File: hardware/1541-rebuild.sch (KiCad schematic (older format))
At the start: 12 parts, among them IC1 ATMEGA1284P-P, J1 ISP, J2 KEYS, J3 EXT_5V, J4 RESET CONN, J5 PC7, SW1 RESET, X1 24Mhz

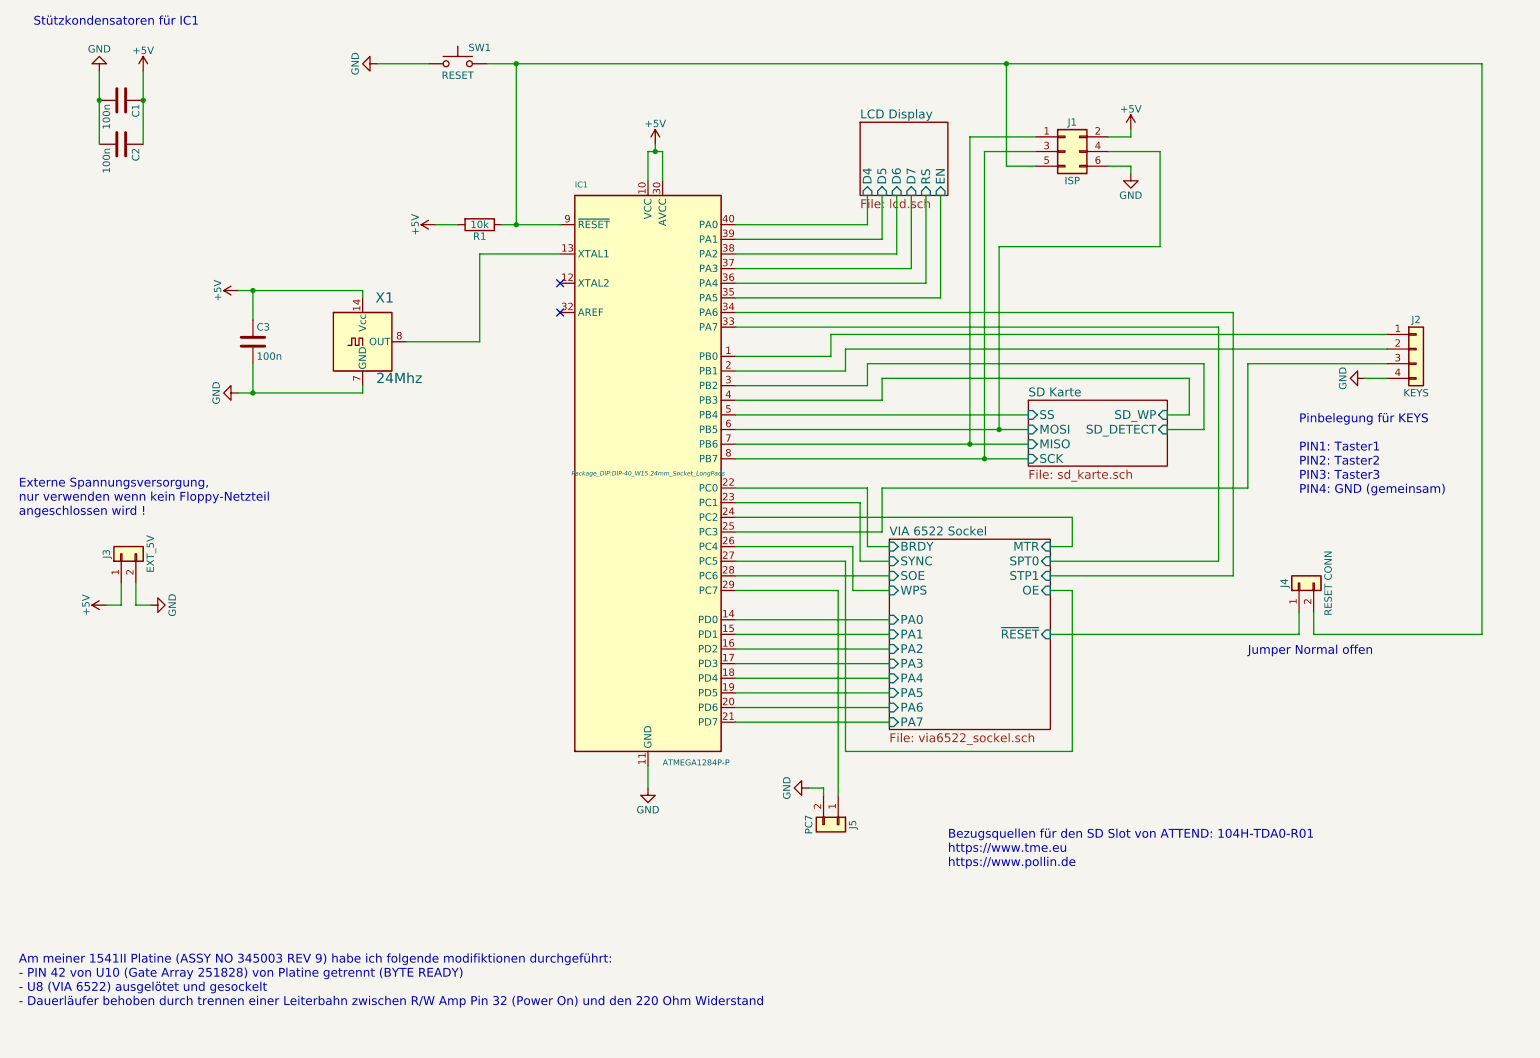
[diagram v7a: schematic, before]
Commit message: Schaltplan angepasst: - SD Card Slot entfernt - SD Card Modul Connector hinzugefügt - im PCB alle Leiterbahne entfernt
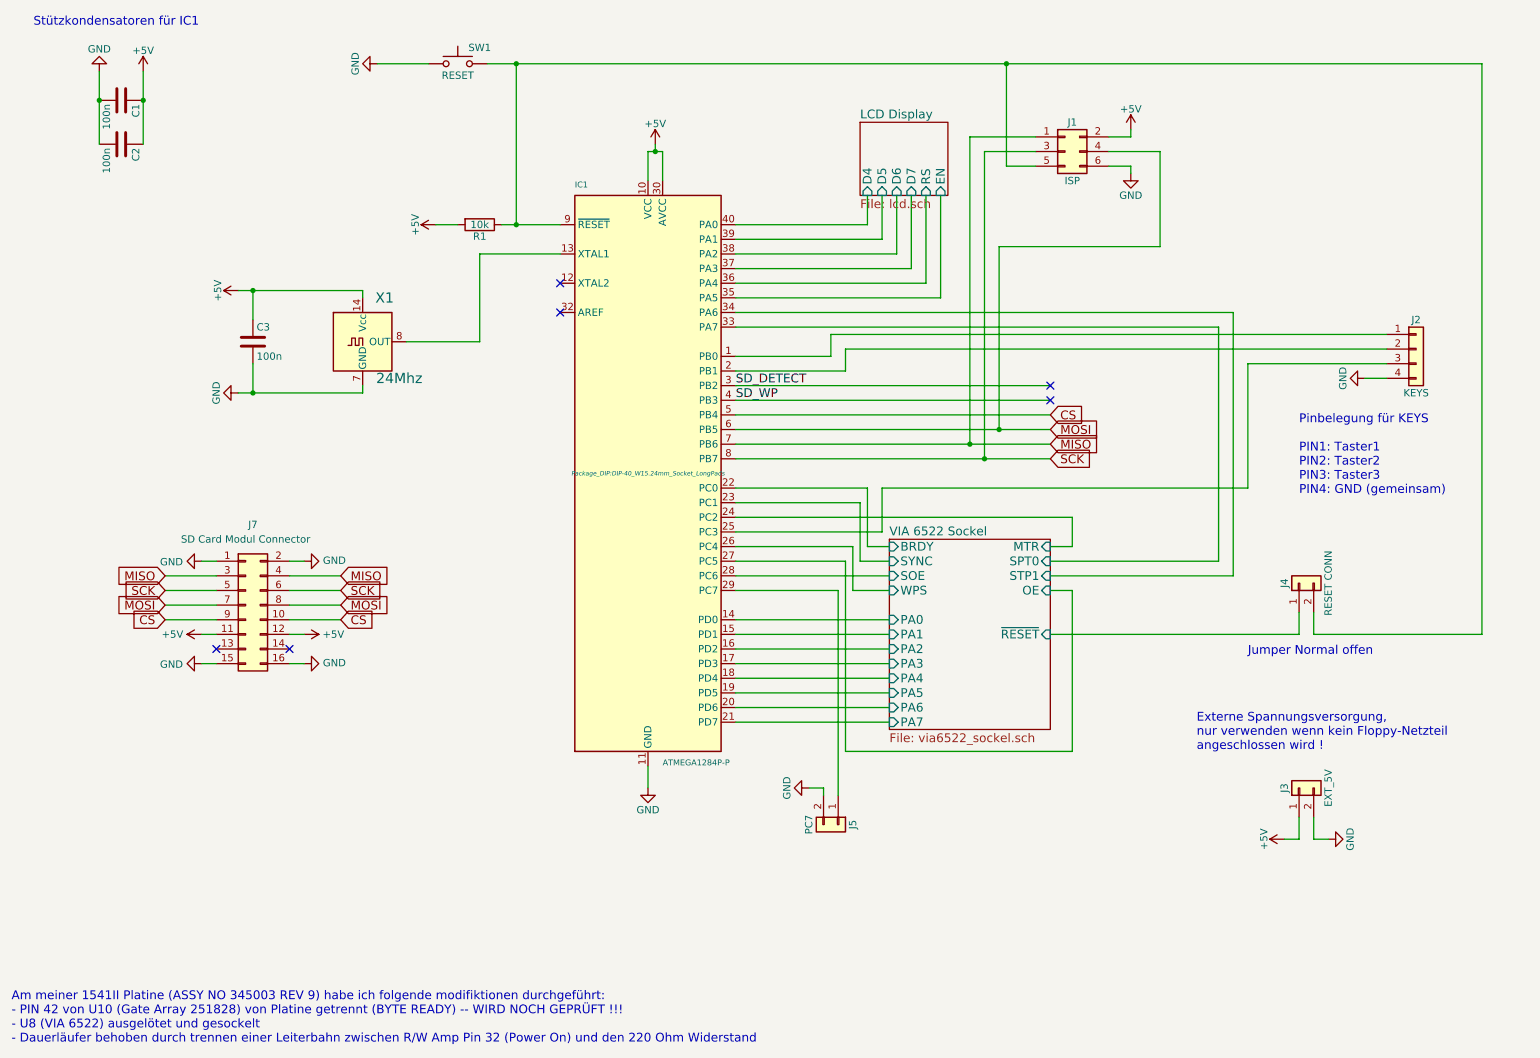
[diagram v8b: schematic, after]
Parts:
- added J7: SD Card Modul Connector, Connector_PinSocket_2.54mm:PinSocket_2x08_P2.54mm_Vertical, symbol Connector_Generic:Conn_02x08_Odd_Even
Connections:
- net +5V: now also J7.11 (Pin_11), J7.12 (Pin_12)
- net GND: now also J7.1 (Pin_1), J7.15 (Pin_15), J7.16 (Pin_16), J7.2 (Pin_2)
- net SD Karte/MISO renamed MISO
- net MISO: now also J7.3 (Pin_3), J7.4 (Pin_4)
- net SD Karte/MOSI renamed MOSI
- net MOSI: now also J7.7 (Pin_7), J7.8 (Pin_8)
- net SD Karte/SCK renamed SCK
- net SCK: now also J7.5 (Pin_5), J7.6 (Pin_6)
- net SD Karte/SD_DETECT renamed SD_DETECT
- net SD Karte/SD_WP renamed SD_WP
- net SD Karte/SS renamed CS
- net CS: now also J7.10 (Pin_10), J7.9 (Pin_9)
- no-connect marks 2 -> 6
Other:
- note added: "Am meiner 1541II Platine (ASSY NO 345003 REV 9) habe ich folgende modifiktionen durchgeführt:\n- PIN 42 von U10 (Gate Array 251828) von Platine getrennt (BYTE READY) -- WIRD NOCH GEPRÜFT !!!\n- U8 (VIA 6522) ausgelötet und gesockelt\n- Dauerläufer behoben durch trennen einer Leiterbahn zwischen R/W Amp Pin 32 (Power On) und den 220 Ohm Widerstand"
- note removed: "Am meiner 1541II Platine (ASSY NO 345003 REV 9) habe ich folgende modifiktionen durchgeführt:\n- PIN 42 von U10 (Gate Array 251828) von Platine getrennt (BYTE READY)\n- U8 (VIA 6522) ausgelötet und gesockelt\n- Dauerläufer behoben durch trennen einer Leiterbahn zwischen R/W Amp Pin 32 (Power On) und den 220 Ohm Widerstand"
- note removed: "Bezugsquellen für den SD Slot von ATTEND: 104H-TDA0-R01\nhttps://www.tme.eu\nhttps://www.pollin.de\n"
- moved on the sheet: J3
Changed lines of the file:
@@
 $Descr A4 11693 8268
 encoding utf-8
-Sheet 1 4
+Sheet 1 3
 Title "1541-rebuid"
 Date "2020-04-14"
@@
 	1    0    0    -1
 $EndComp
-Text Notes 650  7450 0    60   ~ 0
-Am meiner 1541II Platine (ASSY NO 345003 REV 9) habe ich folgende modifiktionen durchgeführt:\n- PIN 42 von U10 (Gate Array 251828) von Platine getrennt (BYTE READY)\n- U8 (VIA 6522) ausgelötet und gesockelt\n- Dauerläufer behoben durch trennen einer Leiterbahn zwischen R/W Amp Pin 32 (Power On) und den 220 Ohm Widerstand
+Text Notes 600  7700 0    60   ~ 0
+Am meiner 1541II Platine (ASSY NO 345003 REV 9) habe ich folgende modifiktionen durchgeführt:\n- PIN 42 von U10 (Gate Array 251828) von Platine getrennt (BYTE READY) -- WIRD NOCH GEPRÜFT !!!\n- U8 (VIA 6522) ausgelötet und gesockelt\n- Dauerläufer behoben durch trennen einer Leiterbahn zwischen R/W Amp Pin 32 (Power On) und den 220 Ohm Widerstand
 $Comp
 L Oscillator:TCXO-14 X1
@@
 Text Notes 750  750  0    60   ~ 0
 Stützkondensatoren für IC1
-$Sheet
-S 7550 3300 950  450
-U 55F7A0F9
-F0 "SD Karte" 60
-F1 "sd_karte.sch" 60
-F2 "MISO" I L 7550 3600 60
-F3 "SCK" I L 7550 3700 60
-F4 "MOSI" I L 7550 3500 60
-F5 "SS" I L 7550 3400 60
-F6 "SD_DETECT" I R 8500 3500 60
-F7 "SD_WP" I R 8500 3400 60
-$EndSheet
 $Sheet
 S 6400 1400 600  500
@@
 	7850 4300 7700 4300
 Wire Wire Line
-	5550 3400 7550 3400
+	5550 3400 7700 3400
 Wire Wire Line
 	5550 3500 7350 3500
@@
 	5550 3700 7250 3700
 Wire Wire Line
-	5550 3300 6550 3300
-Wire Wire Line
-	6550 3300 6550 3150
-Wire Wire Line
-	6550 3150 8650 3150
-Wire Wire Line
-	8650 3150 8650 3400
-Wire Wire Line
-	8650 3400 8500 3400
-Wire Wire Line
-	5550 3200 6450 3200
-Wire Wire Line
-	6450 3200 6450 3050
-Wire Wire Line
-	6450 3050 8750 3050
-Wire Wire Line
-	8750 3050 8750 3500
-Wire Wire Line
-	8750 3500 8500 3500
+	5550 3300 7700 3300
+Wire Wire Line
+	5550 3200 7700 3200
 Wire Wire Line
 	5550 3000 6200 3000
@@
 Wire Wire Line
 	6300 3100 6300 2950
-Wire Wire Line
-	6300 2950 10000 2950
 Wire Wire Line
 	5550 4200 6550 4200
@@
 L Connector_Generic:Conn_01x02 J3
 U 1 1 5AEF69AF
-P 1350 4350
-F 0 "J3" H 1350 4450 50  0000 C CNN
-F 1 "EXT_5V" H 1350 4150 50  0000 C CNN
-F 2 "Connector_PinHeader_2.54mm:PinHeader_1x02_P2.54mm_Vertical" H 1350 4350 50  0001 C CNN
-F 3 "" H 1350 4350 50  0001 C CNN
-	1    1350 4350
+P 9400 5950
+F 0 "J3" H 9400 6050 50  0000 C CNN
+F 1 "EXT_5V" H 9400 5750 50  0000 C CNN
+F 2 "Connector_PinHeader_2.54mm:PinHeader_1x02_P2.54mm_Vertical" H 9400 5950 50  0001 C CNN
+F 3 "" H 9400 5950 50  0001 C CNN
+	1    9400 5950
 	0    -1   -1   0
 $EndComp
@@
 L power:+5V #PWR06
 U 1 1 5AEF757D
-P 1250 4700
-F 0 "#PWR06" H 1250 4550 50  0001 C CNN
-F 1 "+5V" H 1250 4840 50  0000 C CNN
-F 2 "" H 1250 4700 60  0000 C CNN
-F 3 "" H 1250 4700 60  0000 C CNN
-	1    1250 4700
-	0    -1   -1   0
-$EndComp
-Wire Wire Line
-	1350 4550 1350 4700
-Wire Wire Line
-	1450 4700 1450 4550
-Wire Wire Line
-	1350 4700 1250 4700
-Wire Wire Line
-	1450 4700 1550 4700
-Text Notes 650  4100 0    60   ~ 0
+P 9300 6300
+F 0 "#PWR06" H 9300 6150 50  0001 C CNN
+F 1 "+5V" H 9300 6440 50  0000 C CNN
+F 2 "" H 9300 6300 60  0000 C CNN
+F 3 "" H 9300 6300 60  0000 C CNN
+	1    9300 6300
+	0    -1   -1   0
+$EndComp
+Wire Wire Line
+	9400 6150 9400 6300
+Wire Wire Line
+	9500 6300 9500 6150
+Wire Wire Line
+	9400 6300 9300 6300
+Wire Wire Line
+	9500 6300 9600 6300
+Text Notes 8700 5700 0    60   ~ 0
 Externe Spannungsversorgung,\nnur verwenden wenn kein Floppy-Netzteil\nangeschlossen wird !
 Wire Wire Line
@@
 L power:GND #PWR010
 U 1 1 5AF0A9E7
-P 1550 4700
-F 0 "#PWR010" H 1550 4450 50  0001 C CNN
-F 1 "GND" H 1550 4550 50  0000 C CNN
-F 2 "" H 1550 4700 50  0001 C CNN
-F 3 "" H 1550 4700 50  0001 C CNN
-	1    1550 4700
+P 9600 6300
+F 0 "#PWR010" H 9600 6050 50  0001 C CNN
+F 1 "GND" H 9600 6150 50  0000 C CNN
+F 2 "" H 9600 6300 50  0001 C CNN
+F 3 "" H 9600 6300 50  0001 C CNN
+	1    9600 6300
 	0    -1   -1   0
 $EndComp
@@
 Wire Wire Line
 	6150 5950 6150 6000
-Text Notes 7000 6500 0    60   ~ 0
-Bezugsquellen für den SD Slot von ATTEND: 104H-TDA0-R01\nhttps://www.tme.eu\nhttps://www.pollin.de\n
 Wire Wire Line
 	5000 1600 5050 1600
@@
 	1500 1250 1500 1550
 Wire Wire Line
-	7150 3600 7550 3600
-Wire Wire Line
-	7250 3700 7550 3700
+	7150 3600 7700 3600
+Wire Wire Line
+	7250 3700 7700 3700
 Wire Wire Line
 	4050 2100 4350 2100
 Wire Wire Line
-	7350 3500 7550 3500
+	7350 3500 7700 3500
 Wire Wire Line
 	7400 1000 10650 1000
@@
 Wire Wire Line
 	2250 3250 3000 3250
+Wire Wire Line
+	6300 2950 10000 2950
+$Comp
+L Connector_Generic:Conn_02x08_Odd_Even J7
+U 1 1 5E991479
+P 2200 4700
+F 0 "J7" H 2250 5250 50  0000 C CNN
+F 1 "SD Card Modul Connector" H 2200 5150 50  0000 C CNN
+F 2 "Connector_PinSocket_2.54mm:PinSocket_2x08_P2.54mm_Vertical" H 2200 4700 50  0001 C CNN
+F 3 "~" H 2200 4700 50  0001 C CNN
+	1    2200 4700
+	1    0    0    -1
+$EndComp
+Text GLabel 1650 4500 0    60   Input ~ 0
+MISO
+Text GLabel 2850 4500 2    60   Input ~ 0
+MISO
+Wire Wire Line
+	1650 4500 2000 4500
+Wire Wire Line
+	2500 4500 2850 4500
+$Comp
+L power:GND #PWR0106
+U 1 1 5E9BBC13
+P 2600 5100
+F 0 "#PWR0106" H 2600 4850 50  0001 C CNN
+F 1 "GND" V 2605 4972 50  0000 R CNN
+F 2 "" H 2600 5100 50  0001 C CNN
+F 3 "" H 2600 5100 50  0001 C CNN
+	1    2600 5100
+	0    -1   -1   0
+$EndComp
+$Comp
+L power:GND #PWR0107
+U 1 1 5E9BC3F8
+P 1900 5100
+F 0 "#PWR0107" H 1900 4850 50  0001 C CNN
+F 1 "GND" V 1905 4972 50  0000 R CNN
+F 2 "" H 1900 5100 50  0001 C CNN
+F 3 "" H 1900 5100 50  0001 C CNN
+	1    1900 5100
+	0    1    1    0
+$EndComp
+$Comp
+L power:GND #PWR0108
+U 1 1 5E9BC951
+P 1900 4400
+F 0 "#PWR0108" H 1900 4150 50  0001 C CNN
+F 1 "GND" V 1905 4272 50  0000 R CNN
+F 2 "" H 1900 4400 50  0001 C CNN
+F 3 "" H 1900 4400 50  0001 C CNN
+	1    1900 4400
+	0    1    1    0
+$EndComp
+$Comp
+L power:GND #PWR0109
+U 1 1 5E9BCBA4
+P 2600 4400
+F 0 "#PWR0109" H 2600 4150 50  0001 C CNN
+F 1 "GND" V 2605 4272 50  0000 R CNN
+F 2 "" H 2600 4400 50  0001 C CNN
+F 3 "" H 2600 4400 50  0001 C CNN
+	1    2600 4400
+	0    -1   -1   0
+$EndComp
+Wire Wire Line
+	1900 4400 2000 4400
+Wire Wire Line
+	2500 4400 2600 4400
+Wire Wire Line
+	2500 5100 2600 5100
+Wire Wire Line
+	1900 5100 2000 5100
+Text GLabel 1650 4600 0    60   Input ~ 0
+SCK
+Text GLabel 2850 4600 2    60   Input ~ 0
+SCK
+Text GLabel 1650 4700 0    60   Input ~ 0
+MOSI
+Text GLabel 2850 4700 2    60   Input ~ 0
+MOSI
+Text GLabel 1650 4800 0    60   Input ~ 0
+CS
+Text GLabel 2850 4800 2    60   Input ~ 0
+CS
+$Comp
+L power:+5V #PWR0110
+U 1 1 5E9D1262
+P 1900 4900
+F 0 "#PWR0110" H 1900 4750 50  0001 C CNN
+F 1 "+5V" V 1900 5100 50  0000 C CNN
+F 2 "" H 1900 4900 60  0000 C CNN
+F 3 "" H 1900 4900 60  0000 C CNN
+	1    1900 4900
+	0    -1   -1   0
+$EndComp
+$Comp
+L power:+5V #PWR0111
+U 1 1 5E9D1A0B
+P 2600 4900
+F 0 "#PWR0111" H 2600 4750 50  0001 C CNN
+F 1 "+5V" V 2600 5100 50  0000 C CNN
+F 2 "" H 2600 4900 60  0000 C CNN
+F 3 "" H 2600 4900 60  0000 C CNN
+	1    2600 4900
+	0    1    1    0
+$EndComp
+NoConn ~ 2500 5000
+NoConn ~ 2000 5000
+Wire Wire Line
+	2500 4900 2600 4900
+Wire Wire Line
+	1900 4900 2000 4900
+Wire Wire Line
+	1650 4800 2000 4800
+Wire Wire Line
+	2500 4800 2850 4800
+Wire Wire Line
+	2500 4600 2850 4600
+Wire Wire Line
+	2850 4700 2500 4700
+Wire Wire Line
+	2000 4600 1650 4600
+Wire Wire Line
+	2000 4700 1650 4700
+Text GLabel 7700 3700 2    60   Input ~ 0
+SCK
+Text GLabel 7700 3600 2    60   Input ~ 0
+MISO
+Text GLabel 7700 3500 2    60   Input ~ 0
+MOSI
+Text GLabel 7700 3400 2    60   Input ~ 0
+CS
+Text Label 5550 3200 0    60   ~ 0
+SD_DETECT
+Text Label 5550 3300 0    60   ~ 0
+SD_WP
+NoConn ~ 7700 3200
+NoConn ~ 7700 3300
 $EndSCHEMATC
